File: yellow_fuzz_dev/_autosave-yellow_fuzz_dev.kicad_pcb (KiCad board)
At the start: 2 copper layers, 148 parts, among them CON1 SN49B12B, J1 PJ-202A, J2 RA49B11, Q1 DMN2041L, Q10 BC817-25-TP, Q11 NSVJ3910SB3T1GOSCT-ND, Q12 BC817-25-TP, Q13 BC817-25-TP, Q14 NSVJ3910SB3T1GOSCT-ND, Q2 NSVJ3910SB3T1GOSCT-ND, Q3 DMN2041L, Q4 NSVJ3910SB3T1GOSCT-ND, Q5 BC817-25-TP, Q6 BC817-25-TP, Q7 BC817-25-TP, Q8 BC817-25-TP, Q9 BC817-25-TP, SW1 SW_SP3T_A24JP, SW2 SW_SP3T_A24JP, SW3 SW_SP3T_A24JP, SW4 SW_SPST_A11JP, SW5 SW_SPST_A11JP, U1 TL072CP, U2 TL072CP, U3 TL072CP, U4 TL072CP

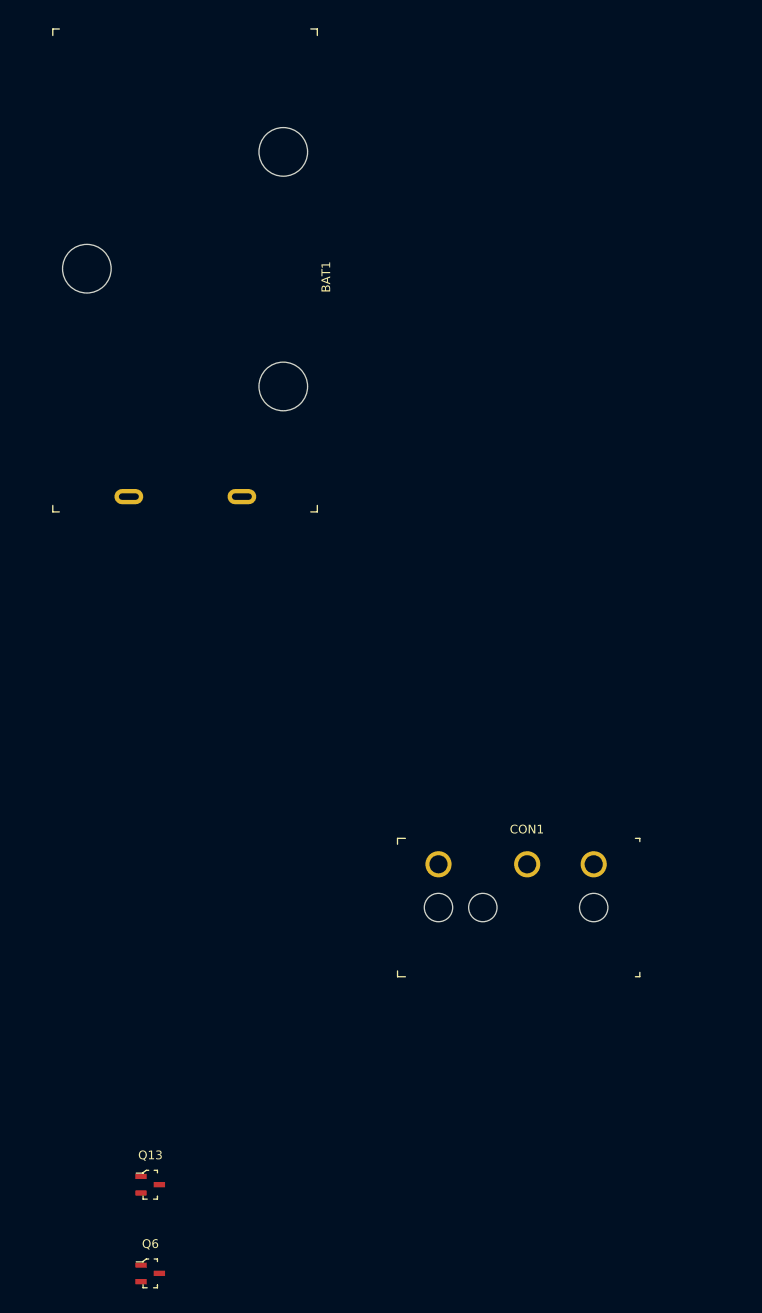
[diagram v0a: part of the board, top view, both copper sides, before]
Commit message: moved footprints into PCB
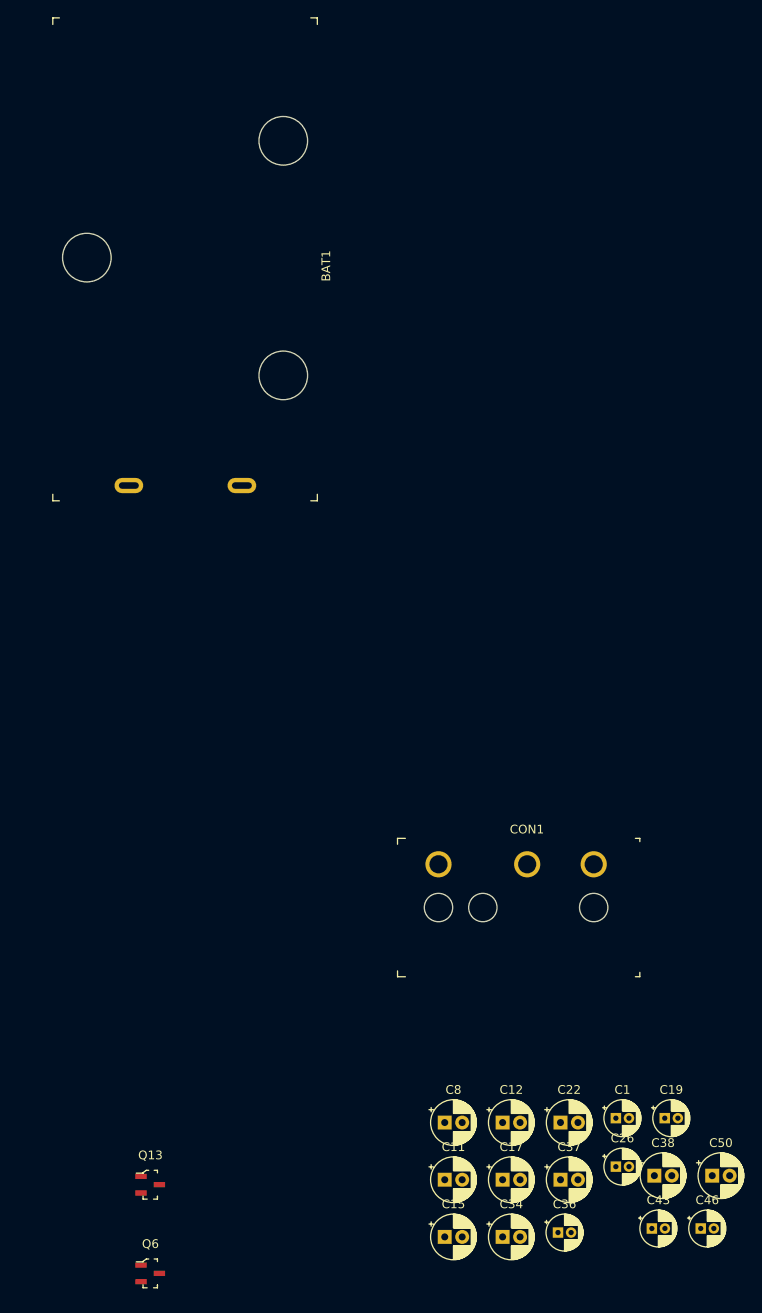
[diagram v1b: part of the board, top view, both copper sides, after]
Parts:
- added C1: 1u, Capacitor_THT:CP_Radial_D4.0mm_P1.50mm, F.Cu at (350.5, 99.1)
- added C11: 100u, Capacitor_THT:CP_Radial_D5.0mm_P2.00mm, F.Cu at (330.9, 106.1)
- added C12: 100u, Capacitor_THT:CP_Radial_D5.0mm_P2.00mm, F.Cu at (337.5, 99.6)
- added C15: 10u, Capacitor_THT:CP_Radial_D5.0mm_P2.00mm, F.Cu at (330.9, 112.7)
- added C17: 10u, Capacitor_THT:CP_Radial_D5.0mm_P2.00mm, F.Cu at (337.5, 106.1)
- added C19: 1u, Capacitor_THT:CP_Radial_D4.0mm_P1.50mm, F.Cu at (356.1, 99.1)
- added C22: 220n, Capacitor_THT:CP_Radial_D5.0mm_P2.00mm, F.Cu at (344.2, 99.6)
- added C26: 1u, Capacitor_THT:CP_Radial_D4.0mm_P1.50mm, F.Cu at (350.5, 104.6)
- added C34: 10u, Capacitor_THT:CP_Radial_D5.0mm_P2.00mm, F.Cu at (337.5, 112.7)
- added C36: 1u, Capacitor_THT:CP_Radial_D4.0mm_P1.50mm, F.Cu at (343.9, 112.2)
- added C37: 10u, Capacitor_THT:CP_Radial_D5.0mm_P2.00mm, F.Cu at (344.2, 106.1)
- added C38: 220n, Capacitor_THT:CP_Radial_D5.0mm_P2.00mm, F.Cu at (354.9, 105.6)
- added C43: 1u, Capacitor_THT:CP_Radial_D4.0mm_P1.50mm, F.Cu at (354.6, 111.7)
- added C46: 1u, Capacitor_THT:CP_Radial_D4.0mm_P1.50mm, F.Cu at (360.2, 111.7)
- added C50: 10u, Capacitor_THT:CP_Radial_D5.0mm_P2.00mm, F.Cu at (361.6, 105.6)
- added C8: 100u, Capacitor_THT:CP_Radial_D5.0mm_P2.00mm, F.Cu at (330.9, 99.6)
- moved BAT1 1.27 mm to (312.4, 14.0)
